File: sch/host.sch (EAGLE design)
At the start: 10 parts

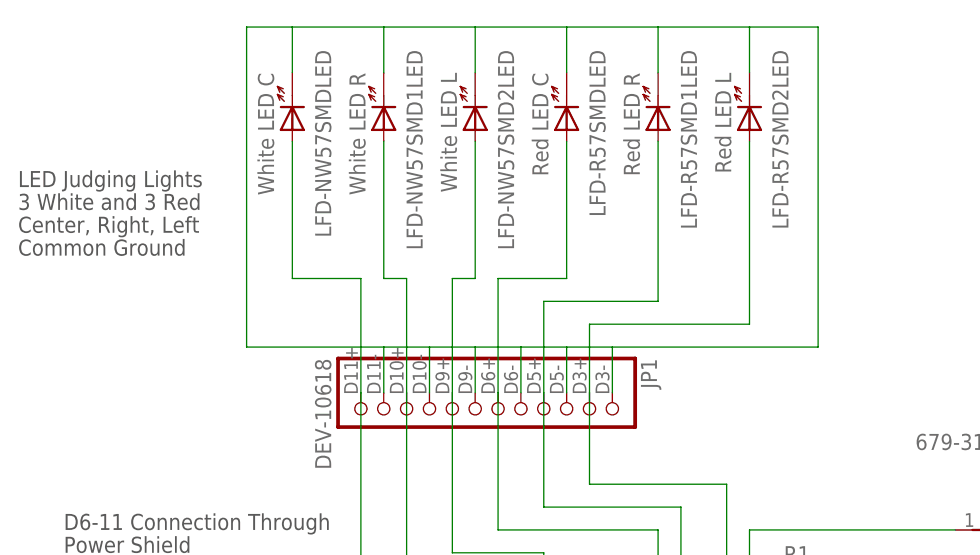
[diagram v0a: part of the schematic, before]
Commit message: Updated readme, correct host LED connections in schematic, added Xbee programmer to BOM.
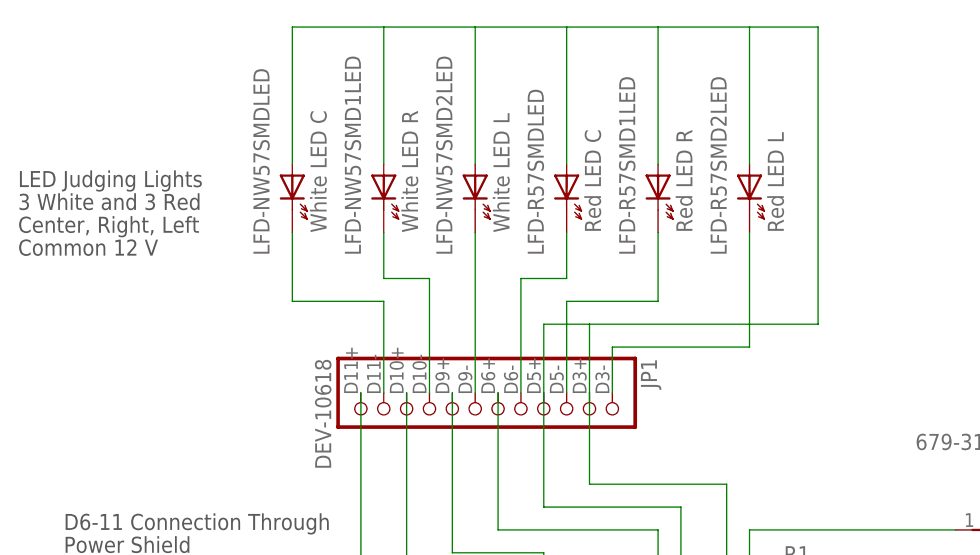
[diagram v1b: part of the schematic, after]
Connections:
- removed net N$10: JP1.D10-, JP1.D11-, JP1.D3-, JP1.D5-, JP1.D6-, JP1.D9-, LFD-NW57SMD1LED.K, LFD-NW57SMD2LED.K, LFD-NW57SMDLED.K, LFD-R57SMD1LED.K, LFD-R57SMD2LED.K, LFD-R57SMDLED.K
- new net N$15: JP1.D3-, LFD-R57SMD2LED.K
- new net N$16: JP1.D11-, LFD-NW57SMDLED.K
- new net N$18: JP1.D10-, LFD-NW57SMD1LED.K
- new net N$20: JP1.D6-, LFD-R57SMDLED.K
- new net N$21: JP1.D5-, LFD-R57SMD1LED.K
- net N$3: now also JP1.D9-, LFD-NW57SMD2LED.K; no longer JP1.D3+, LFD-R57SMD2LED.A, PCB1.~3
- net N$4: now also JP1.D3+, LFD-NW57SMD1LED.A, LFD-NW57SMD2LED.A, LFD-NW57SMDLED.A, LFD-R57SMD2LED.A, LFD-R57SMDLED.A, PCB1.~3
- net N$5: no longer LFD-R57SMDLED.A
- net N$6: no longer LFD-NW57SMD2LED.A
- net N$7: no longer LFD-NW57SMD1LED.A
- net N$8: no longer LFD-NW57SMDLED.A
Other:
- note added: "Common 12 V"
- note removed: "Common Ground"
- moved on the sheet: LFD-NW57SMD1LED, LFD-NW57SMD2LED, LFD-NW57SMDLED, LFD-R57SMD1LED, LFD-R57SMD2LED, LFD-R57SMDLED

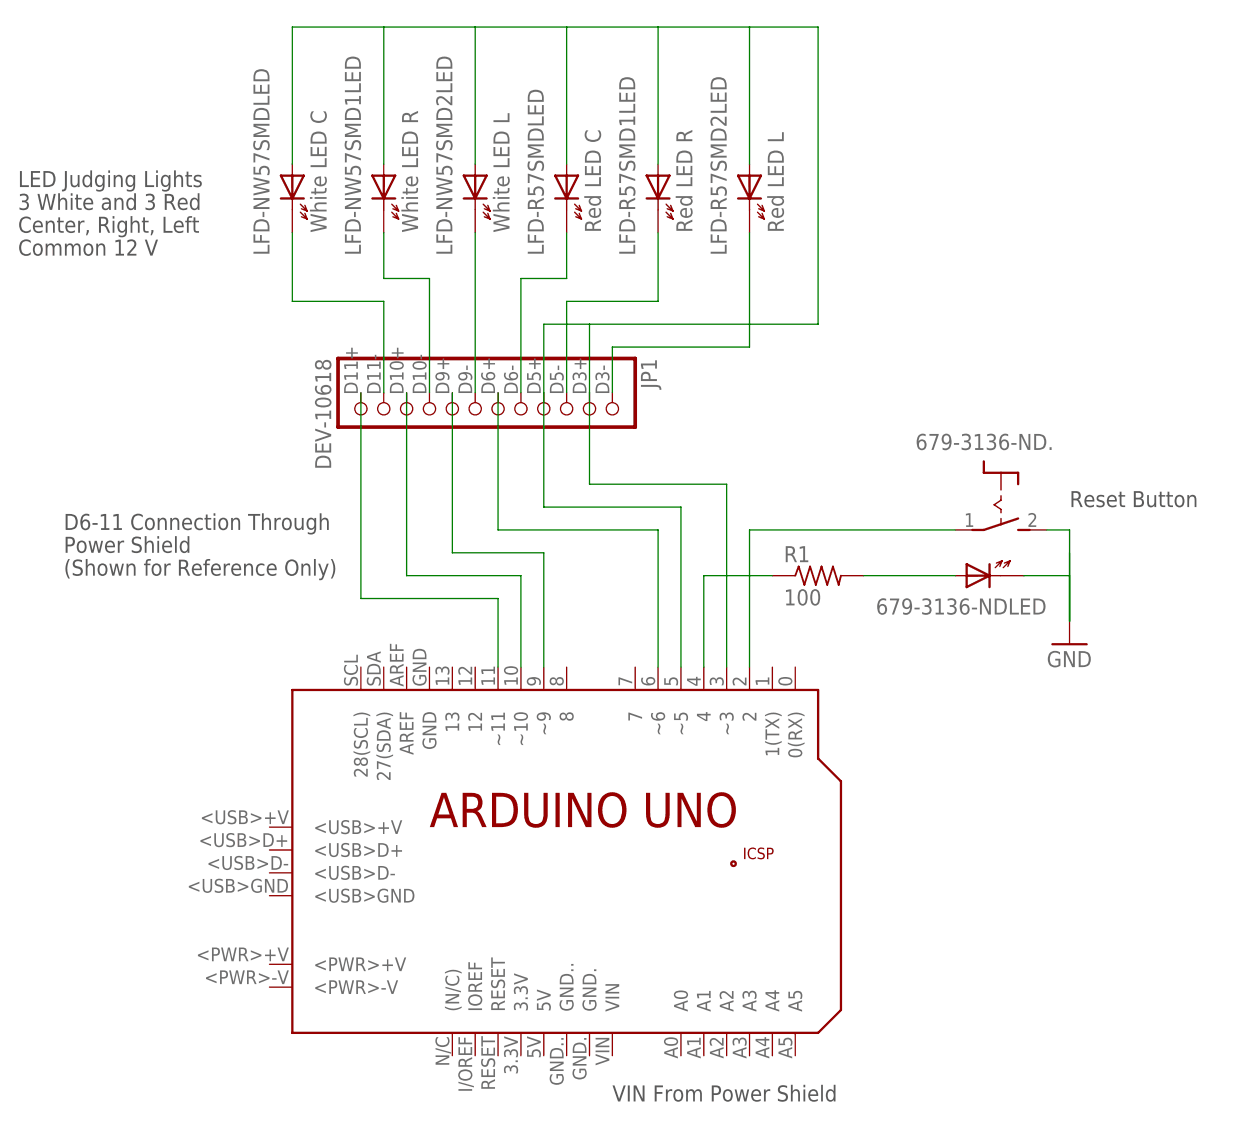
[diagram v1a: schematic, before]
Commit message: Cleaned up schematics, more clearly labeled.
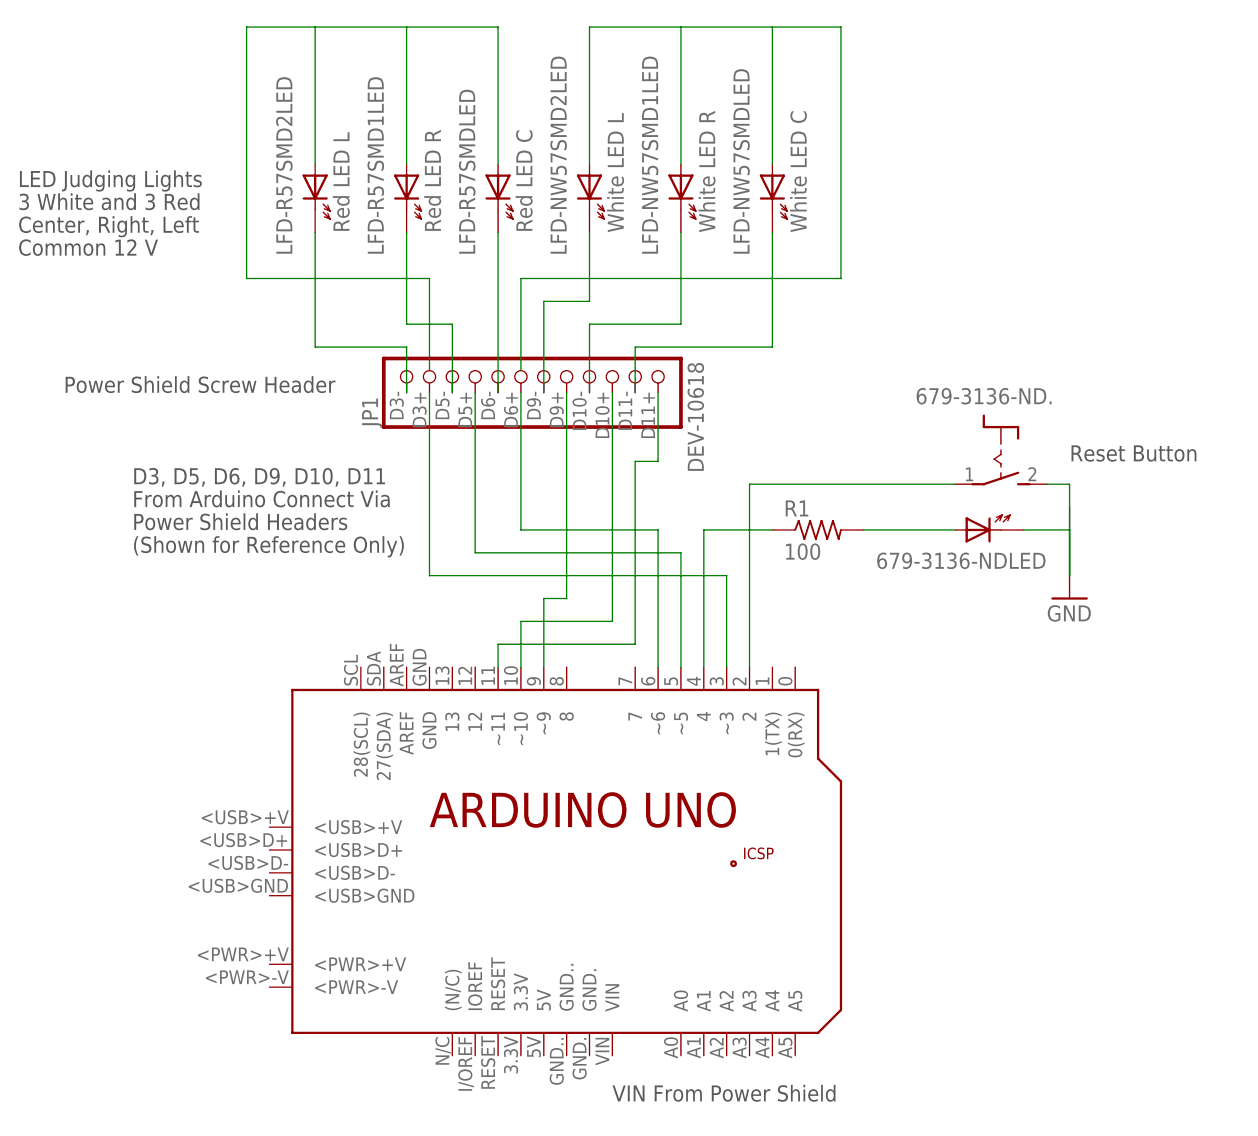
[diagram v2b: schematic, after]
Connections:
- removed net N$4 (its old number): JP1.D3+, JP1.D5+, LFD-NW57SMD1LED.A, LFD-NW57SMD2LED.A, LFD-NW57SMDLED.A, LFD-R57SMD1LED.A, LFD-R57SMD2LED.A, LFD-R57SMDLED.A, PCB1.~3, PCB1.~5
- new net N$16: LFD-R57SMD1LED.A, LFD-R57SMD2LED.A, LFD-R57SMDLED.A
- new net N$17: LFD-NW57SMD1LED.A, LFD-NW57SMD2LED.A, LFD-NW57SMDLED.A
- new net N$6: JP1.D3+, PCB1.~3
- new net N$7: JP1.D5+, PCB1.~5
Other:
- note added: "D3, D5, D6, D9, D10, D11"
- note added: "From Arduino Connect Via"
- note added: "Power Shield Headers"
- note added: "Power Shield Screw Header"
- note removed: "D6-11 Connection Through"
- note removed: "Power Shield"
- moved on the sheet: 679-3136-ND., 679-3136-NDLED, JP1, LFD-NW57SMD1LED, LFD-NW57SMD2LED, LFD-NW57SMDLED, LFD-R57SMD1LED, LFD-R57SMD2LED, LFD-R57SMDLED, R1
